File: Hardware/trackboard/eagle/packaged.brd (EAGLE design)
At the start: 160 x 100 mm, 41 parts, among them Q1 BS170, U1 ADNS-3080, X9.00 RESON

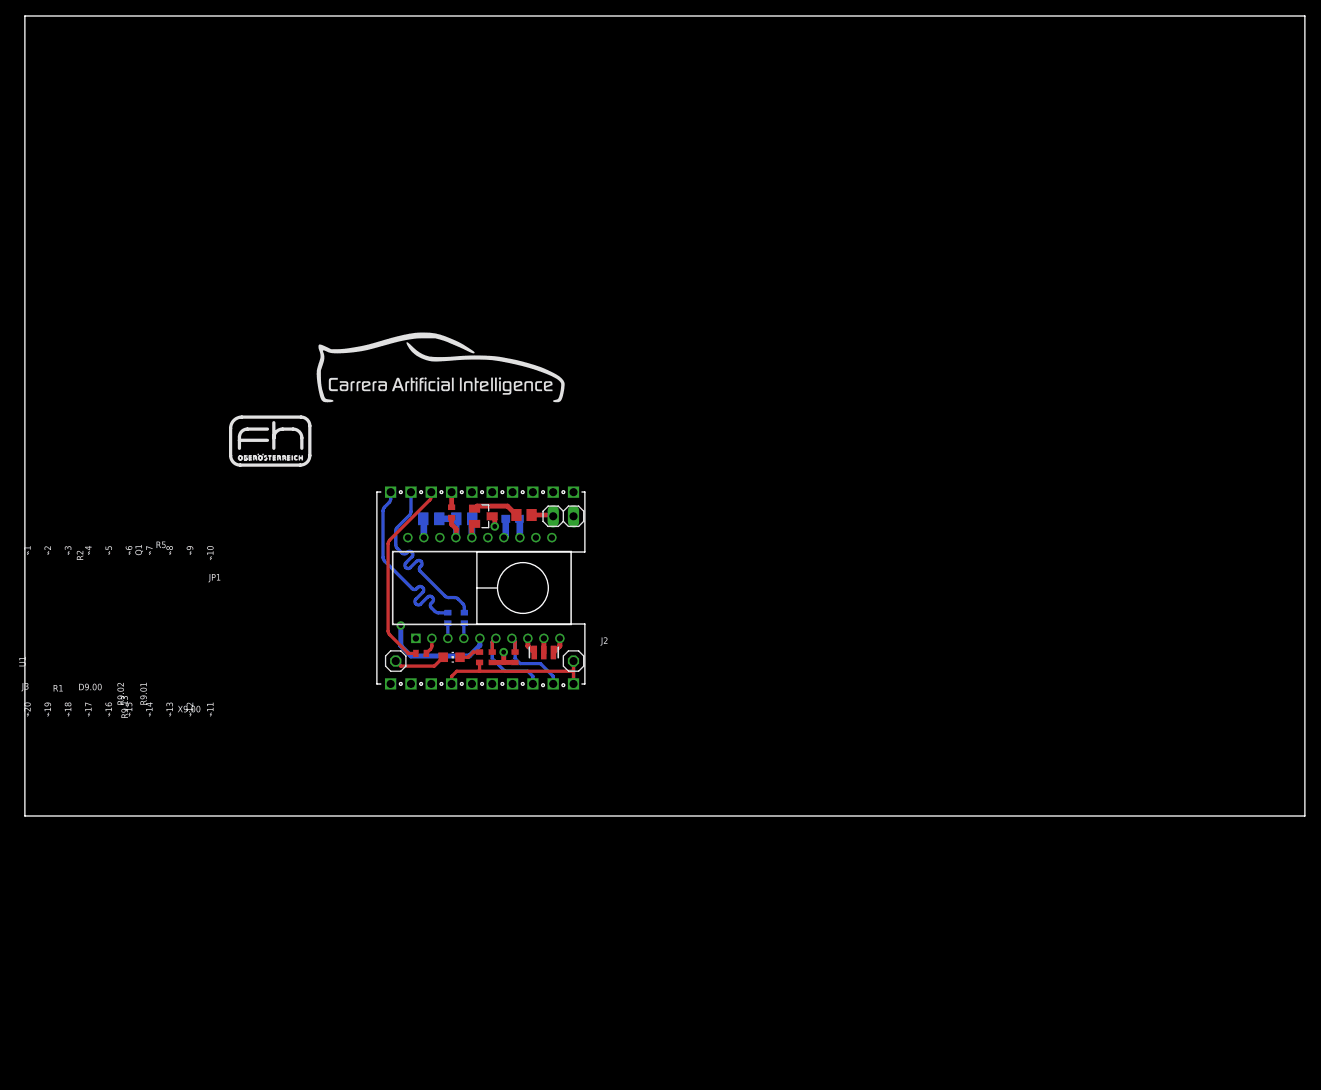
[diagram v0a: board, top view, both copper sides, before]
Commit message: packaged adns3080 submodule/sublayout into an importable pair of files
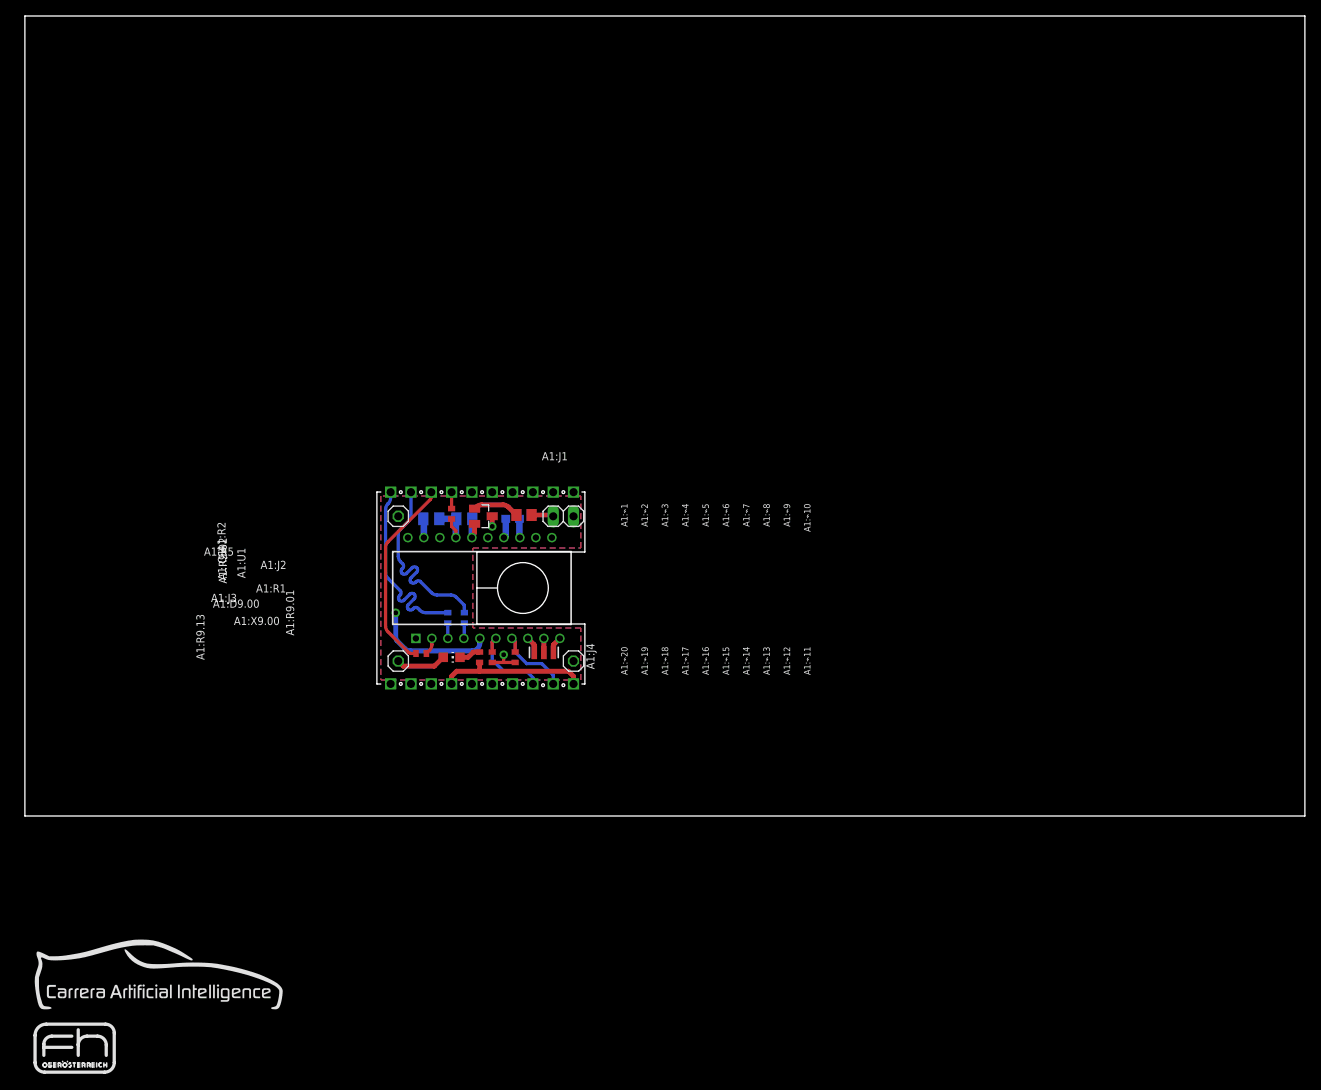
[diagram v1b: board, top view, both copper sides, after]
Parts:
- removed DCL1: DCL.CARRERAI, kitt.refs:DCL.LOGO-CARRERAI.W30MM
- removed DCL2: DCL.OSH.COPPER'5MM', kitt.refs:DCL.LOGO-OSH.5MM
- removed J3: (no value), pinhead:1X01
- removed R2: 10kR, rcl:R0402
- removed REF1: REF.LOGO.UASUA, kitt.refs:REF_LOGO_UASUA
- removed U1: ADNS-3080, kitt.ic:ADNS-3080
- removed X9.00: RESON, Ai_Passives:RESON-SMD
- added A1:DCL1: DCL.CARRERAI, kitt.refs:DCL.LOGO-CARRERAI.W30MM
- added A1:DCL2: DCL.OSH.COPPER'5MM', kitt.refs:DCL.LOGO-OSH.5MM
- added A1:J2, A1:J3: (no value), pinhead:1X01
- added A1:R2: 10kR, rcl:R0402
- added A1:REF1: REF.LOGO.UASUA, kitt.refs:REF_LOGO_UASUA
- added A1:U1: ADNS-3080, kitt.ic:ADNS-3080
- added A1:X9.00: RESON, Ai_Passives:RESON-SMD
- renumbered C9.03 to A1:C9.03, C9.04 to A1:C9.05, C9.05 to A1:C9.04, D9.00 to A1:D9.00, J2 to A1:J4, JP1 to A1:J1, Q1 to A1:Q1, R1 to A1:R1, R3 to A1:R3, R4 to A1:R4, R5 to A1:R5, R9.01 to A1:R9.01, R9.02 to A1:R9.02, R9.13 to A1:R9.13, ⌁1 to A1:⌁1, ⌁10 to A1:⌁10, ⌁11 to A1:⌁11, ⌁12 to A1:⌁12, ⌁13 to A1:⌁13, ⌁14 to A1:⌁14, ⌁15 to A1:⌁15, ⌁16 to A1:⌁16, ⌁17 to A1:⌁17, ⌁18 to A1:⌁18, ⌁19 to A1:⌁19, ⌁2 to A1:⌁2, ⌁20 to A1:⌁20, ⌁3 to A1:⌁3, ⌁4 to A1:⌁4, ⌁5 to A1:⌁5, ⌁6 to A1:⌁6, ⌁7 to A1:⌁7, ⌁8 to A1:⌁8, ⌁9 to A1:⌁9
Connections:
- net !CS1 renamed A1:!CS1
- net !INT renamed A1:!INT
- net GPIO1 renamed A1:GPIO1
- net GPIO2 renamed A1:GPIO2
- net GPIO3 renamed A1:GPIO3
- net MISO renamed A1:MISO
- net MOSI renamed A1:MOSI
- net N$11 renamed A1:N$11
- net N$7 renamed A1:N$7
- net N$8 renamed A1:N$8
- net SCL renamed A1:SCL
- net SCLK renamed A1:SCLK
- net SDA renamed A1:SDA
- net V++ renamed A1:V++
- removed net !CS0: A1:⌁4.X, R2.2, U1.1
- removed net !PD: A1:R9.01.2, A1:⌁12.X, U1.7
- removed net +3V3: A1:C9.04.1, A1:C9.05.1, A1:D9.00.A, A1:J1.1, A1:R9.01.1, A1:R9.02.1, A1:⌁10.X, J3.1, R2.1, U1.12, U1.15, U1.17
- removed net GND: A1:C9.04.2, A1:C9.05.2, A1:J4.1, A1:Q1.2, A1:R9.13.2, A1:⌁11.X, A1:⌁17.X, A1:⌁9.X, U1.16, U1.19
- removed net N$1: U1.9, X9.00.2
- removed net N$2: U1.8, X9.00.3
- removed net N$3: U1.10, X9.00.1
- removed net N$4: A1:Q1.3, U1.5
- removed net N$5: A1:C9.03.1, U1.13
- removed net N$6: A1:C9.03.2, U1.14
- removed net N$9: U1.20
- removed net RST: A1:R9.02.2, A1:⌁13.X, U1.6
- removed net U1.MISO: A1:R1.2, U1.2
- removed net U1.MOSI: A1:R4.2, U1.4
- removed net U1.SCLK: A1:R3.2, U1.3
- new net A1:!CS0: A1:R2.2, A1:U1.1, A1:⌁4.X
- new net A1:!PD: A1:R9.01.2, A1:U1.7, A1:⌁12.X
- new net A1:+3V3: A1:C9.04.1, A1:C9.05.1, A1:D9.00.A, A1:J1.1, A1:J3.1, A1:J4.1, A1:R2.1, A1:R9.01.1, A1:R9.02.1, A1:U1.12, A1:U1.15, A1:U1.17, A1:⌁10.X
- new net A1:+5V: A1:⌁18.X
- new net A1:GND: A1:C9.04.2, A1:C9.05.2, A1:J2.1, A1:Q1.2, A1:R9.13.2, A1:U1.16, A1:U1.19, A1:⌁11.X, A1:⌁17.X, A1:⌁9.X
- new net A1:N$1: A1:U1.9, A1:X9.00.2
- new net A1:N$2: A1:U1.8, A1:X9.00.3
- new net A1:N$3: A1:U1.10, A1:X9.00.1
- new net A1:N$4: A1:Q1.3, A1:U1.5
- new net A1:N$5: A1:C9.03.1, A1:U1.13
- new net A1:N$6: A1:C9.03.2, A1:U1.14
- new net A1:N$9: A1:U1.20
- new net A1:RST: A1:R9.02.2, A1:U1.6, A1:⌁13.X
- new net A1:U1.MISO: A1:R1.2, A1:U1.2
- new net A1:U1.MOSI: A1:R4.2, A1:U1.4
- new net A1:U1.SCLK: A1:R3.2, A1:U1.3
- new net A1:VSYS: A1:⌁19.X
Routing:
- net N$4: track 42.5 -> 0.00 mm, vias 2 -> 0
- net A1:N$4: track 0.00 -> 38.8 mm, vias 0 -> 2
- net !CS0: track 31.5 -> 0.00 mm
- net A1:!CS0: track 0.00 -> 30.6 mm
- net GND: track 29.9 -> 0.00 mm
- net A1:GND: track 0.00 -> 25.4 mm
- net +3V3: track 18.1 -> 0.00 mm, vias 1 -> 0
- net A1:+3V3: track 0.00 -> 17.3 mm, vias 0 -> 1
- net RST: track 11.6 -> 0.00 mm
- net A1:RST: track 0.00 -> 11.5 mm
- net !PD: track 11.2 -> 0.00 mm
- net A1:!PD: track 0.00 -> 10.8 mm
- net A1:N$6: track 0.00 -> 2.45 mm
- net N$6: track 2.45 -> 0.00 mm
- net A1:N$5: track 0.00 -> 2.37 mm
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- added copper zone on layer 15, net A1:+3V3
- added copper zone on layer 2, net A1:GND
- added copper zone on layer 16, net A1:GND1
- added copper zone on layer 1, net A1:GND2
- removed copper zone on layer 15, net +3V3
- removed copper zone on layer 2, net GND

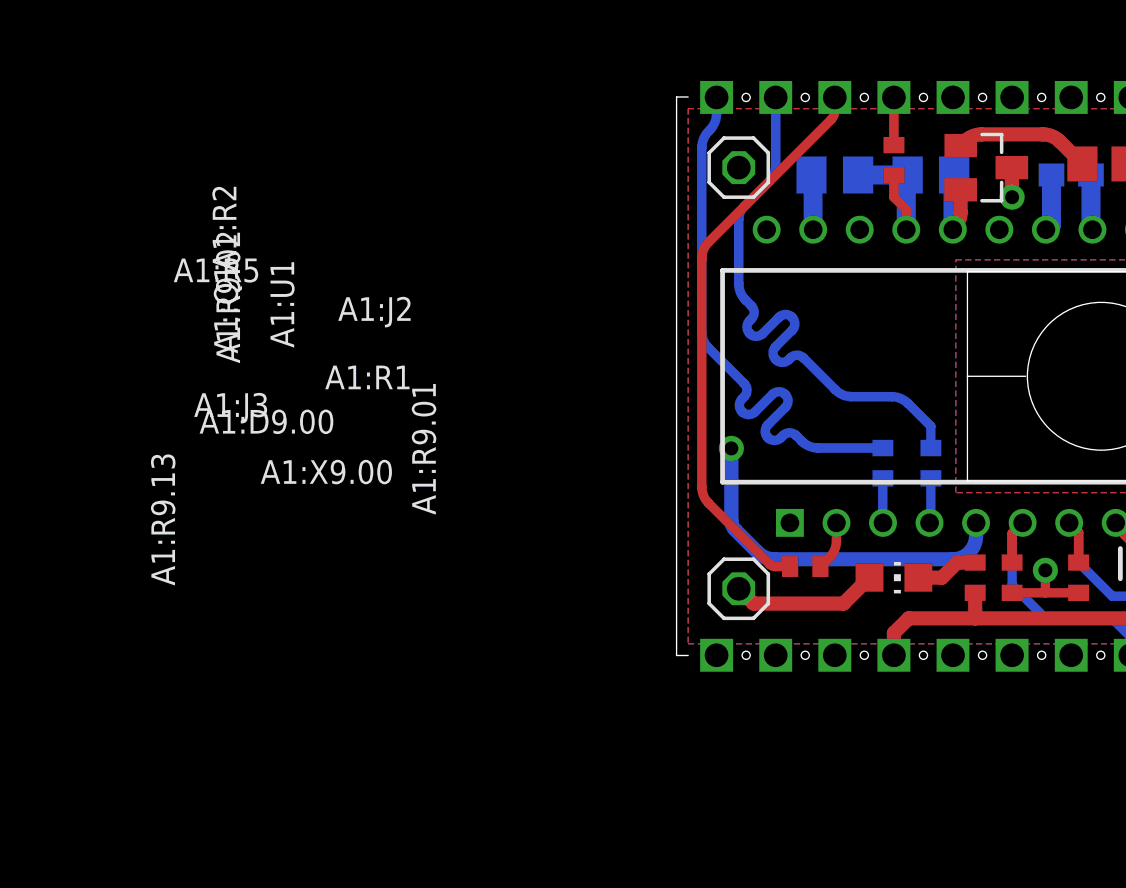
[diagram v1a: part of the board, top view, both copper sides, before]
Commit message: renamed some designators (now trying some hacking to remove ugly colon-based prefixes eagle tries to force)
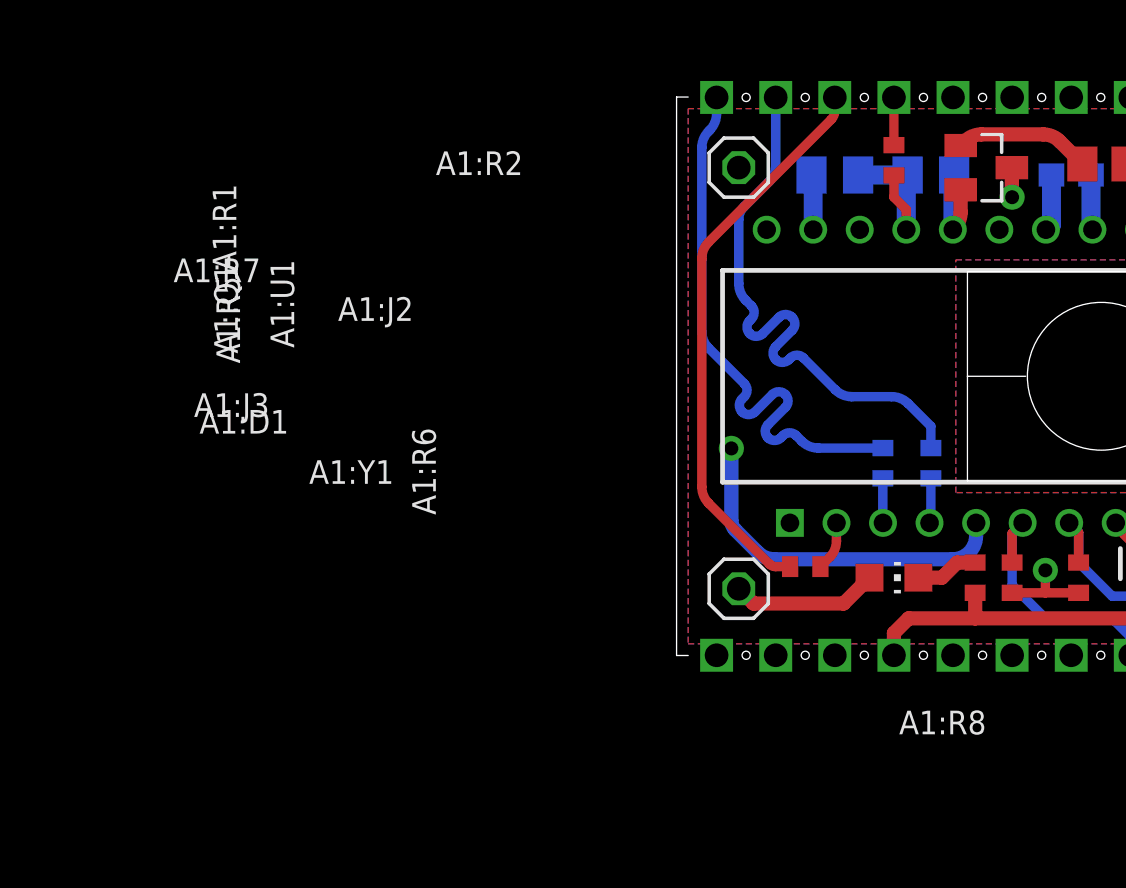
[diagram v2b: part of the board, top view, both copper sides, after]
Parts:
- removed A1:R9.02: 10kR, rcl:R0402
- added A1:R7: 200R, rcl:R0805
- A1:C1: value 2.2uF -> 2.2uF/⇤
- A1:C2, A1:C3: value 100nF -> 100nF/⇤
- A1:R1: value 100R -> 10kR/⎒
- A1:R2: value 10kR -> 100R/⇤
- A1:R3, A1:R4: value 100R -> 100R/⇤
- A1:R5: value (none) -> 10kR/⎒; device rcl:R0805 -> rcl:R0402
- A1:R6: value 10kR -> 10kR/⎒
- A1:R8: value [PPR] -> 10kR
- A1:Y1: value RESON -> 24MHz
- moved A1:R5 18.2 mm to (58.4, 19.8), turned to 90 degrees
- moved A1:R1 17.9 mm to (53.3, 37.8), turned to 90 degrees
- moved A1:R2 17.9 mm to (49.5, 20.3), turned to 0 degrees
- renumbered A1:C9.03 to A1:C1, A1:C9.04 to A1:C2, A1:C9.05 to A1:C3, A1:D9.00 to A1:D1, A1:R9.01 to A1:R6, A1:R9.13 to A1:R8, A1:X9.00 to A1:Y1
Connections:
- net A1:N$1 renamed A1:U1.GUARD
- net A1:N$2 renamed A1:U1.OSCOUT✳
- net A1:N$3 renamed A1:U1.OSCIN✳
- net A1:!CS0: now also A1:R1.2; no longer A1:R2.2
- net A1:+3V3: now also A1:R1.1, A1:R5.1; no longer A1:R2.1, A1:R9.02.1
- net A1:MISO: now also A1:R2.1; no longer A1:R1.1
- net A1:N$7: now also A1:R7.1; no longer A1:R5.1
- net A1:N$8: now also A1:R7.2; no longer A1:R5.2
- net A1:RST: now also A1:R5.2; no longer A1:R9.02.2
- net A1:U1.MISO: now also A1:R2.2; no longer A1:R1.2

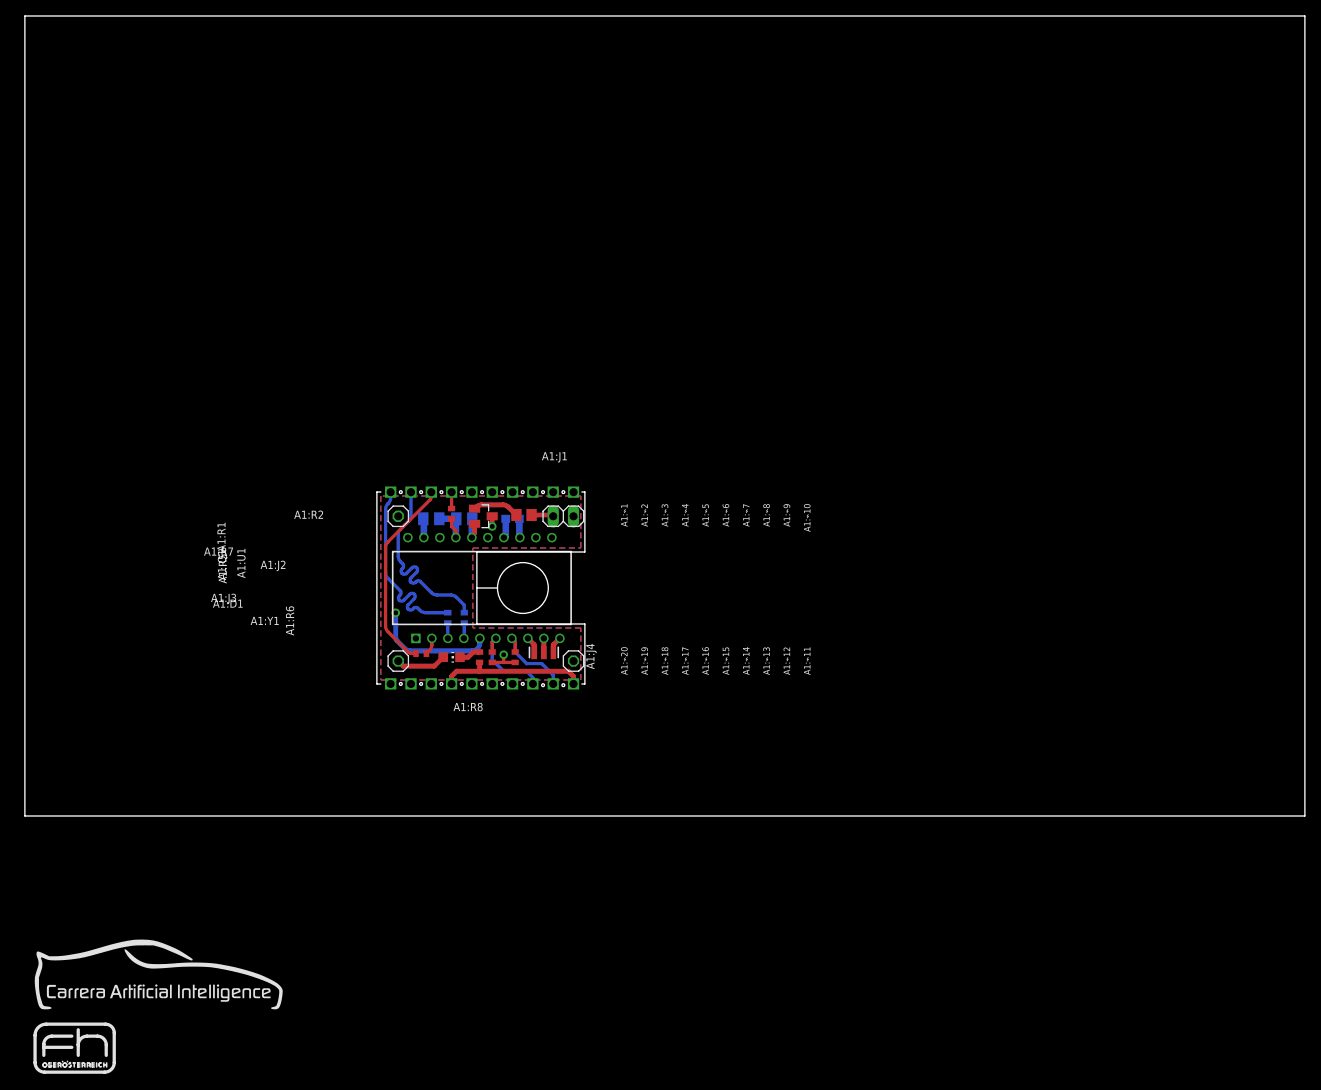
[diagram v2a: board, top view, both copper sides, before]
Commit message: finished silkscreening, checked component values and finalized module packaging ; to import into a design, use the "Import EAGLE drawing" command
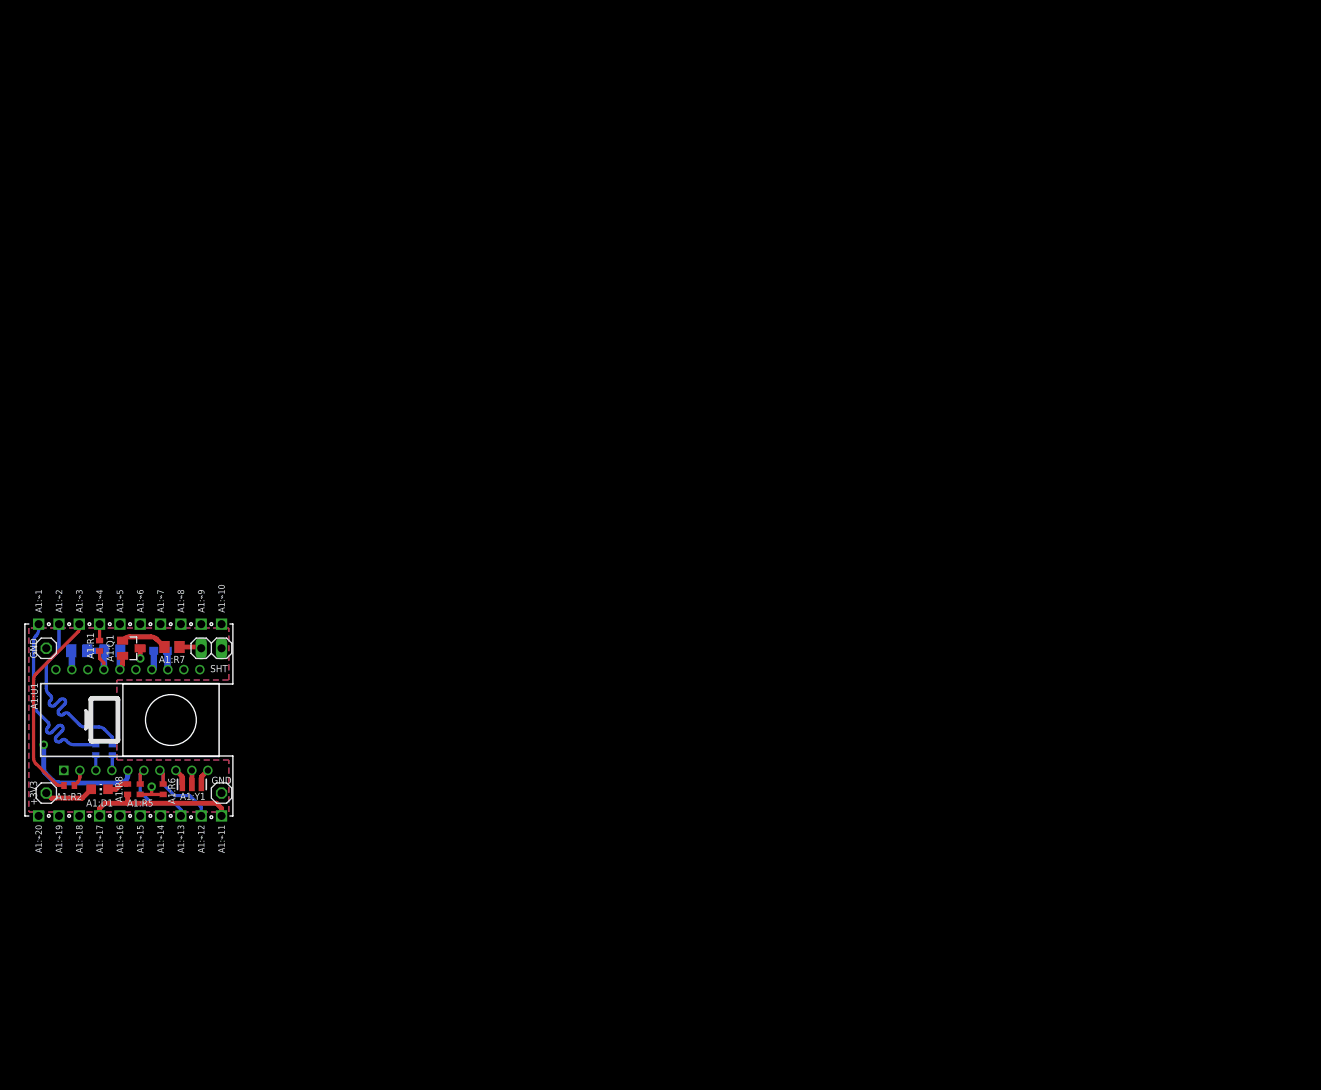
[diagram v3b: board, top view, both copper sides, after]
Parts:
- removed A1:DCL1: DCL.CARRERAI, kitt.refs:DCL.LOGO-CARRERAI.W30MM
- removed A1:REF1: REF.LOGO.UASUA, kitt.refs:REF_LOGO_UASUA
- added A1:U$1: SIGNATURE, decals:SIG_DOMH
- A1:DCL2: value DCL.OSH.COPPER'5MM' -> DCL.OSH'3MM-SLK'; device kitt.refs:DCL.LOGO-OSH.5MM -> kitt.refs:DCL.LOGO-OSH.3MM
- moved A1:DCL2 49.5 mm to (3.62, 15.2), turned to 180 degrees
- moved A1:⌁12 47.0 mm to (22.0, 0.01)
- moved A1:⌁9 47.0 mm to (22.0, 24.0)
- moved A1:C1 47.0 mm to (17.0, 20.6)
- moved A1:C2 47.0 mm to (6.80, 20.6)
- moved A1:C3 47.0 mm to (10.9, 20.6)
- moved A1:D1 47.0 mm to (9.34, 3.34)
- moved A1:J1 47.0 mm to (23.3, 21.0)
- moved A1:J2 47.0 mm to (2.67, 21.0)
- moved A1:J3 47.0 mm to (2.67, 2.87)
- moved A1:J4 47.0 mm to (24.6, 2.87)
- moved A1:Q1 47.0 mm to (13.3, 21.0)
- moved A1:R1 47.0 mm to (9.34, 21.3)
- moved A1:R2 47.0 mm to (5.53, 3.82)
- moved A1:R3 47.0 mm to (8.86, 8.27)
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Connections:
- net A1:+3V3: no longer A1:J4.1
- net A1:GND: now also A1:J4.1
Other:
- board size 160 x 100 mm -> 26 x 24 mm
- board text added: "+3V3"
- board text added: "GND"
- board text added: "HSD'16 CarrerAI"
- board text added: "OSHW SPFMDBC"
- board text added: "P#:KITT-C100'R1"
- board text added: "SHT"
